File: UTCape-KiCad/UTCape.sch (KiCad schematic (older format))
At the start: 5 parts, among them IC1 74LVC1G157

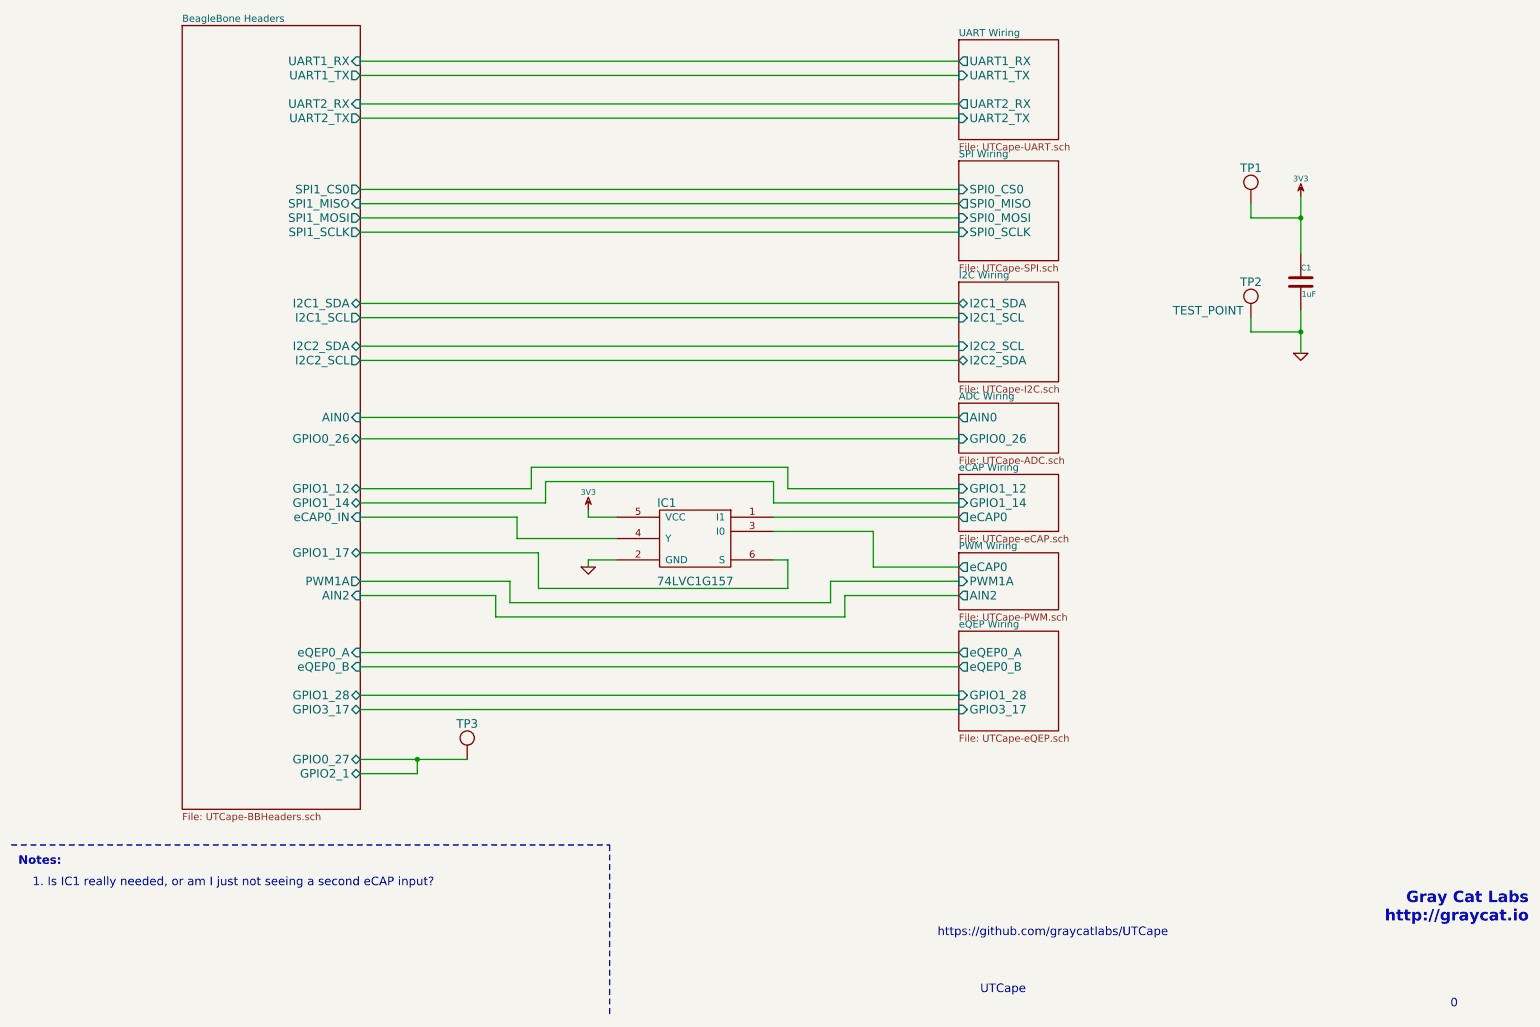
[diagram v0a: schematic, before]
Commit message: layed out PCB, some minor wiring changes for layout
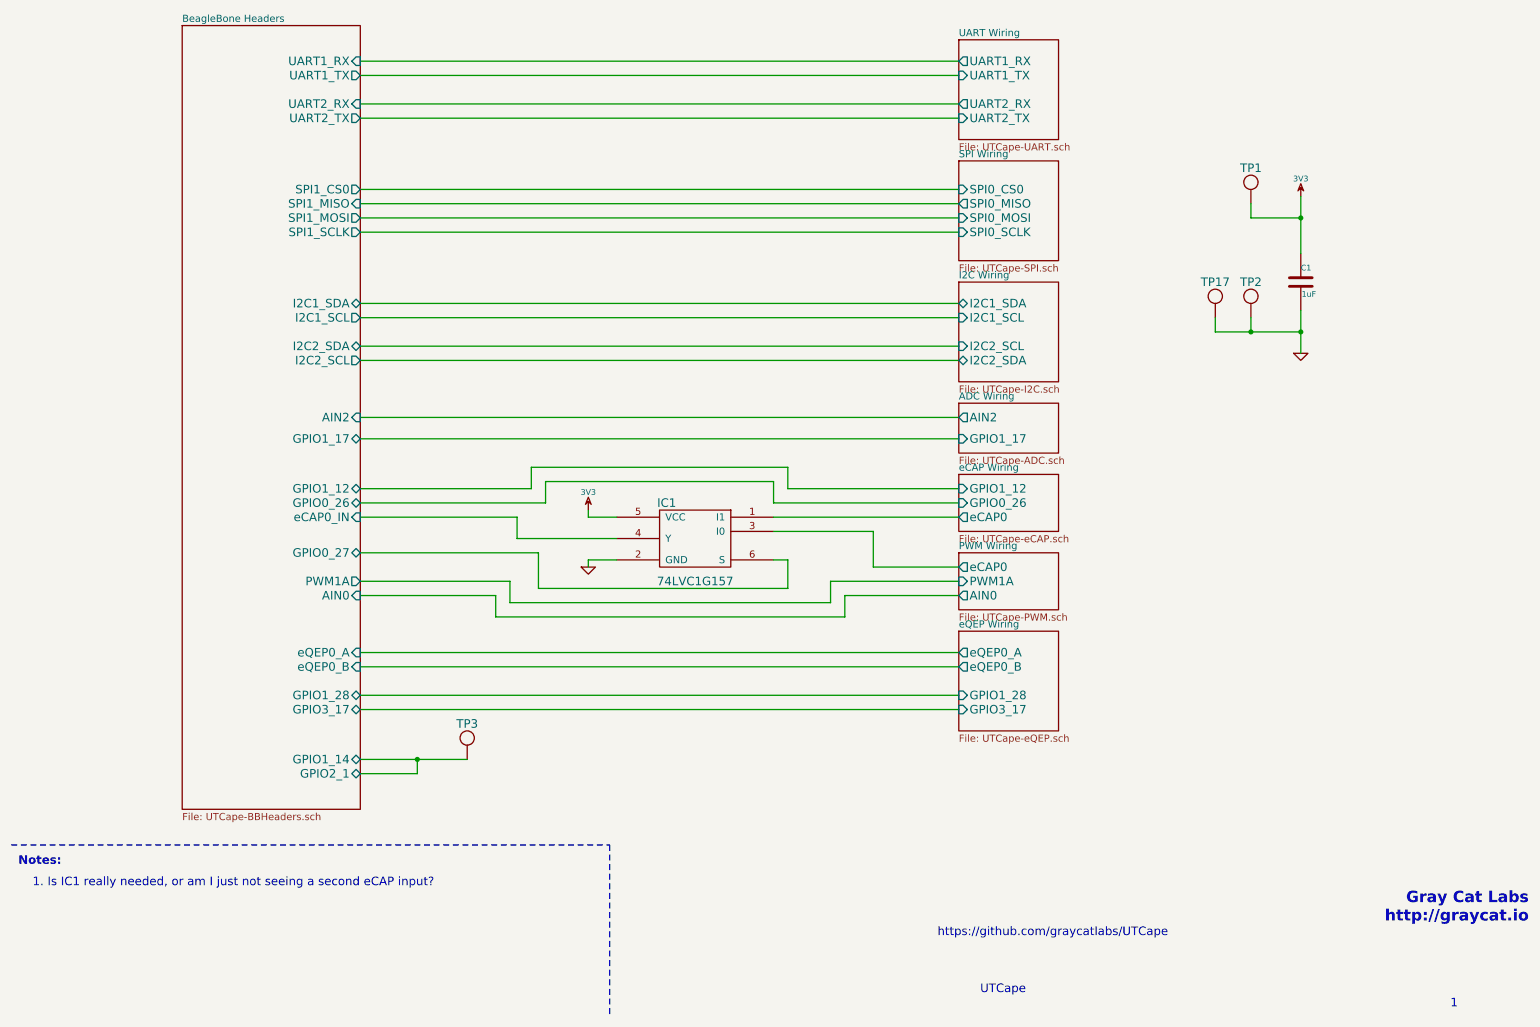
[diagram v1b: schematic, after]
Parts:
- added TP17: TEST_POINT, symbol TEST_POINT
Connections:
- net BeagleBone Headers/GPIO1_17 is gone; now on net BeagleBone Headers/GPIO0_27: IC1.6 (S)
- net BeagleBone Headers/GPIO0_27: no longer TP3.1
- net BeagleBone Headers/GPIO1_14: now also TP3.1
- net GND: now also TP17.1
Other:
- note added: "1"
- note removed: "0"
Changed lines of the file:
@@
 LIBS:contrib
 LIBS:valves
+LIBS:beagleboneblack
 LIBS:GrayCatLabs
-LIBS:BeagleBoneBlack
 LIBS:UTCape-cache
 EELAYER 27 0
@@
 UTCape
 Text Notes 10650 7650 0    60   ~ 0
-0
+1
 $Sheet
 S 7200 850  700  700
@@
 P 9250 2800
 F 0 "TP2" H 9250 3050 60  0000 C CNN
-F 1 "TEST_POINT" H 8950 2850 60  0000 C CNN
+F 1 "TEST_POINT" H 8950 2850 60  0001 C CNN
 F 2 "" H 9250 2800 60  0000 C CNN
 F 3 "" H 9250 2800 60  0000 C CNN
@@
 F0 "ADC Wiring" 50
 F1 "UTCape-ADC.sch" 50
-F2 "AIN0" O L 7200 3500 60
-F3 "GPIO0_26" I L 7200 3650 60
+F2 "GPIO1_17" I L 7200 3650 60
+F3 "AIN2" O L 7200 3500 60
 $EndSheet
 $Sheet
@@
 F1 "UTCape-eCAP.sch" 50
 F2 "GPIO1_12" I L 7200 4000 60
-F3 "GPIO1_14" I L 7200 4100 60
-F4 "eCAP0" O L 7200 4200 60
+F3 "eCAP0" O L 7200 4200 60
+F4 "GPIO0_26" I L 7200 4100 60
 $EndSheet
 $Sheet
@@
 F1 "UTCape-PWM.sch" 50
 F2 "PWM1A" I L 7200 4650 60
-F3 "AIN2" O L 7200 4750 60
-F4 "eCAP0" O L 7200 4550 60
+F3 "eCAP0" O L 7200 4550 60
+F4 "AIN0" O L 7200 4750 60
 $EndSheet
 $Sheet
@@
 F3 "I2C2_SCL" O R 3000 3100 60
 F4 "UART2_TX" O R 3000 1400 60
-F5 "GPIO1_17" B R 3000 4450 60
+F5 "GPIO1_17" B R 3000 3650 60
 F6 "GPIO3_17" B R 3000 5550 60
 F7 "eQEP0_B" I R 3000 5250 60
 F8 "SPI1_MISO" I R 3000 2000 60
 F9 "SPI1_SCLK" O R 3000 2200 60
-F10 "AIN2" I R 3000 4750 60
-F11 "AIN0" I R 3000 3500 60
+F10 "AIN2" I R 3000 3500 60
+F11 "AIN0" I R 3000 4750 60
 F12 "GPIO1_28" B R 3000 5450 60
 F13 "PWM1A" O R 3000 4650 60
@@
 F22 "eCAP0_IN" I R 3000 4200 60
 F23 "GPIO1_12" B R 3000 4000 60
-F24 "GPIO1_14" B R 3000 4100 60
-F25 "GPIO0_26" B R 3000 3650 60
-F26 "GPIO0_27" B R 3000 5900 60
+F24 "GPIO1_14" B R 3000 5900 60
+F25 "GPIO0_26" B R 3000 4100 60
+F26 "GPIO0_27" B R 3000 4450 60
 F27 "GPIO2_1" B R 3000 6000 60
 $EndSheet
@@
 	9600 2750 9600 3050
 Wire Wire Line
-	9600 2900 9250 2900
+	9000 2900 9600 2900
 Wire Wire Line
 	9250 2900 9250 2800
@@
 	3000 4200 4100 4200
 Wire Wire Line
-	3000 4450 4250 4450
-Wire Wire Line
 	4250 4450 4250 4700
 Wire Wire Line
@@
 	6600 4300 5900 4300
 Wire Wire Line
-	3000 4100 4300 4100
-Wire Wire Line
-	4300 4100 4300 3950
-Wire Wire Line
-	4300 3950 5900 3950
-Wire Wire Line
-	5900 3950 5900 4100
-Wire Wire Line
-	5900 4100 7200 4100
-Wire Wire Line
 	7200 4000 6000 4000
 Wire Wire Line
@@
 	4200 4000 3000 4000
 Wire Wire Line
-	3000 3650 7200 3650
-Wire Wire Line
-	3000 3500 7200 3500
-Wire Wire Line
 	7200 4650 6300 4650
 Wire Wire Line
@@
 Wire Wire Line
 	4050 4650 3000 4650
-Wire Wire Line
-	3000 4750 3950 4750
-Wire Wire Line
-	3950 4750 3950 4900
-Wire Wire Line
-	3950 4900 6400 4900
-Wire Wire Line
-	6400 4900 6400 4750
-Wire Wire Line
-	6400 4750 7200 4750
 $Sheet
 S 7200 5000 700  700
@@
 Wire Wire Line
 	3000 1000 7200 1000
-Wire Wire Line
-	3000 5900 3750 5900
-Wire Wire Line
-	3400 5900 3400 6000
-Wire Wire Line
-	3400 6000 3000 6000
 $Comp
 L TEST_POINT TP3
@@
 	1    0    0    -1
 $EndComp
-Connection ~ 3400 5900
 $Bitmap
 Pos 5200 7400
@@
 53 DD DB 70 1F 36 16 E8 FD 00 E2 DF AD 51 CE 83 A6 28 F1 7F 81 8B E0 02 2E 82 F7 7A 32 7C 03 A2
 99 A9 ED 10 75 E1 56 1A 44 BB 99 51 9D 33 AA 2F 6B B6 E7 B9 1B FC 3F 2A D6 C2 F1 E6 45 93 97 00
-00 00 00 49 45 4E 44 AE 42 60 82 EF $EndBitmap
+00 00 00 49 45 4E 44 AE 42 60 82 86 $EndBitmap
 EndData
 $EndBitmap
@@
 03 43 83 61 8C 09 03 03 03 03 43 83 61 8C 09 03 03 03 03 43 83 61 8C 09 03 03 03 03 43 83 61 03
 60 D2 64 32 30 30 30 30 34 84 CF 1C 00 A9 00 9C 01 A8 8B 59 19 06 06 06 06 06 E9 E3 33 80 C5 FF
-07 47 25 A5 D2 E9 03 52 D8 00 00 00 00 49 45 4E 44 AE 42 60 82 76 $EndBitmap
+07 47 25 A5 D2 E9 03 52 D8 00 00 00 00 49 45 4E 44 AE 42 60 82 4A $EndBitmap
 EndData
 $EndBitmap
@@
 Text Notes 700  6800 0    60   ~ 0
 1. Is IC1 really needed, or am I just not seeing a second eCAP input?
+$Comp
+L TEST_POINT TP17
+U 1 1 54ECDC94
+P 9000 2800
+F 0 "TP17" H 9000 3050 60  0000 C CNN
+F 1 "TEST_POINT" H 8700 2850 60  0001 C CNN
+F 2 "" H 9000 2800 60  0000 C CNN
+F 3 "" H 9000 2800 60  0000 C CNN
+	1    9000 2800
+	1    0    0    -1
+$EndComp
+Wire Wire Line
+	9000 2900 9000 2800
+Connection ~ 9250 2900
+Wire Wire Line
+	4250 4450 3000 4450
+Wire Wire Line
+	3000 3650 7200 3650
+Wire Wire Line
+	4300 4100 4300 3950
+Wire Wire Line
+	4300 3950 5900 3950
+Wire Wire Line
+	5900 3950 5900 4100
+Wire Wire Line
+	5900 4100 7200 4100
+Wire Wire Line
+	4300 4100 3000 4100
+Wire Wire Line
+	3000 5900 3750 5900
+Wire Wire Line
+	3000 6000 3400 6000
+Wire Wire Line
+	3400 6000 3400 5900
+Connection ~ 3400 5900
+Wire Wire Line
+	3000 3500 7200 3500
+Wire Wire Line
+	3000 4750 3950 4750
+Wire Wire Line
+	3950 4750 3950 4900
+Wire Wire Line
+	3950 4900 6400 4900
+Wire Wire Line
+	6400 4900 6400 4750
+Wire Wire Line
+	6400 4750 7200 4750
 $EndSCHEMATC
